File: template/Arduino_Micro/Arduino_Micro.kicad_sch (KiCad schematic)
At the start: 6 parts, among them P1 Digital, P2 Analog, P3 CONN_01X01, P4 CONN_01X01, P5 CONN_01X01, P6 CONN_01X01

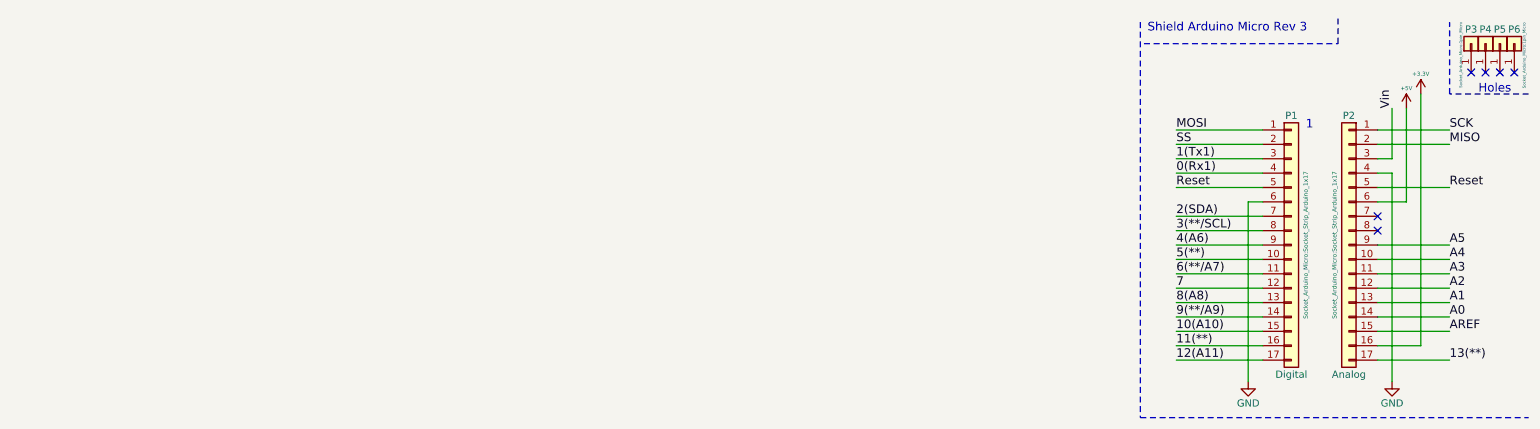
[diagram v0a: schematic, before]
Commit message: fix: change original libs; add: new components
- Fix LIS3DH pins positions;
- Add ATmega164P symbol;
- Add 3D model to the L_Wuerth_HCM-7050;
- Add parameters for R_RES (Assembly...).
- Add parameters for R_RES and C_CAP;
- Fix SOIC-8 package 3D model;
- Add new parameters for many symbols;
- Change text height from 70 mil to 50 mil;
- Add solder mask expansion for 2-contact jumpers;
- Change thermopad vias of QFN-20-1EP_3x3mm_P0.45mm_EP1.6x1.6mm_ThermalVias;
- Add D_SMAF footprint;
- Fillet silk for C_1206;
-Rectangle silk for R_1206;
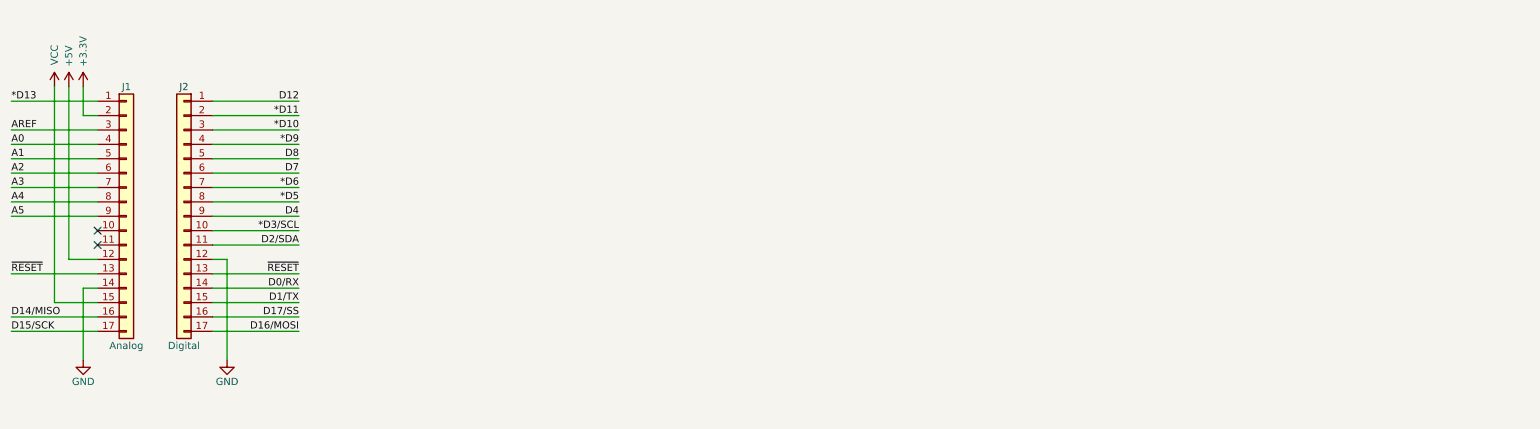
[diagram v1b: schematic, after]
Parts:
- removed P3, P4, P5, P6: CONN_01X01, Socket_Arduino_Micro:1pin_Micro, symbol Connector_Generic:Conn_01x01
- J1: renamed from P1; value Digital -> Analog; footprint Socket_Arduino_Micro:Socket_Strip_Arduino_1x17 -> Connector_PinHeader_2.54mm:PinHeader_1x17_P2.54mm_Vertical
- J2: renamed from P2; value Analog -> Digital; footprint Socket_Arduino_Micro:Socket_Strip_Arduino_1x17 -> Connector_PinHeader_2.54mm:PinHeader_1x17_P2.54mm_Vertical
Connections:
- net 0(Rx1) is gone; now on net A0: J1.4 (Pin_4)
- net 1(Tx1) is gone; now on net AREF: J1.3 (Pin_3)
- net 2(SDA) is gone; now on net A3: J1.7 (Pin_7)
- net 3(**/SCL) is gone; now on net A4: J1.8 (Pin_8)
- net 4(A6) is gone; now on net A5: J1.9 (Pin_9)
- net 7 is gone; now on net +5V: J1.12 (Pin_12)
- net 9(**/A9) is gone; now on net GND: J1.14 (Pin_14)
- net SS is gone; now on net +3V3: J1.2 (Pin_2)
- net +3V3: no longer J2.16 (Pin_16)
- net +5V: no longer J2.6 (Pin_6)
- net A0: no longer J2.14 (Pin_14)
- net A1: now also J1.5 (Pin_5); no longer J2.13 (Pin_13)
- net A2: now also J1.6 (Pin_6); no longer J2.12 (Pin_12)
- net A3: no longer J2.11 (Pin_11)
- net A4: no longer J2.10 (Pin_10)
- net A5: no longer J2.9 (Pin_9)
- net AREF: no longer J2.15 (Pin_15)
- net GND: now also J2.12 (Pin_12); no longer J1.6 (Pin_6), J2.4 (Pin_4)
- net *D6: now reaches J2.7 (Pin_7)
- net *D5: now reaches J2.8 (Pin_8)
- net 10(A10) renamed VCC
- net 11(**) renamed D14/MISO
- net 12(A11) renamed D15/SCK
- net 13(**) renamed D16/MOSI
- net 5(**): no longer names the net of J1.10 (Pin_10)
- net 6(**/A7): no longer names the net of J1.11 (Pin_11)
- net 8(A8) renamed ~{RESET}
- net ~{RESET}: now also J2.13 (Pin_13)
- net MISO renamed *D11
- net MOSI renamed *D13
- net Reset renamed D8
- net D8: no longer J1.5 (Pin_5)
- net SCK renamed D12
- net Vin renamed *D10
- new net *D3/SCL: J2.10 (Pin_10)
- new net *D9: J2.4 (Pin_4)
- new net D0/RX: J2.14 (Pin_14)
- new net D17/SS: J2.16 (Pin_16)
- new net D1/TX: J2.15 (Pin_15)
- new net D2/SDA: J2.11 (Pin_11)
- new net D4: J2.9 (Pin_9)
- new net D7: J2.6 (Pin_6)
- no-connect marks 6 -> 2
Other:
- note removed: "1"
- note removed: "Holes"
- note removed: "Shield Arduino Micro Rev 3"
- moved on the sheet: J1, J2
